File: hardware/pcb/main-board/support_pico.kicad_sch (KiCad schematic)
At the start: 7 parts, among them J702 Z88 SD Card, U701 Support Pico

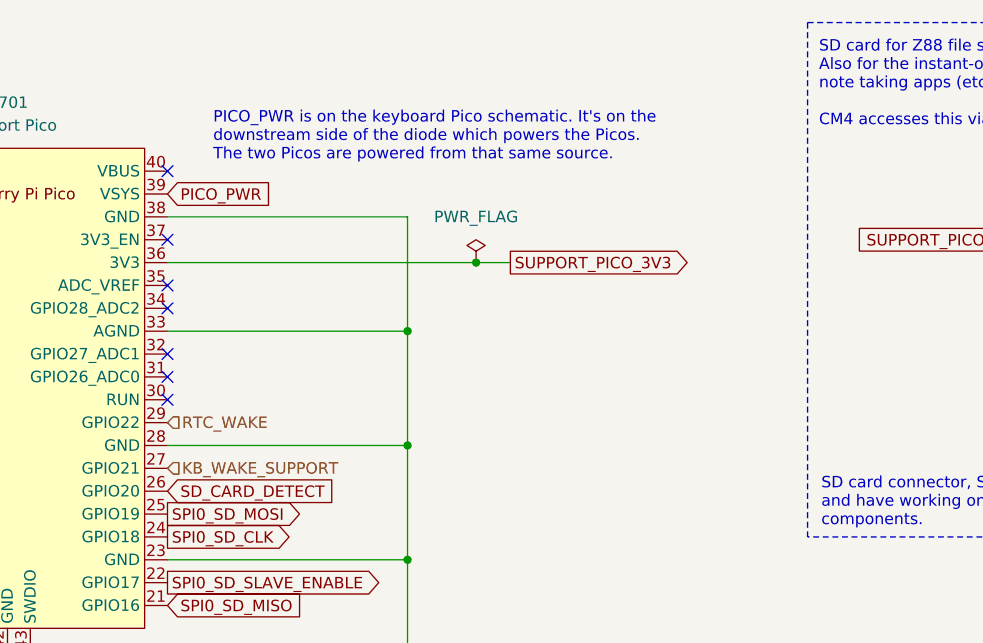
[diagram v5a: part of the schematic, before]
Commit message: more working out of the KB pico replacement
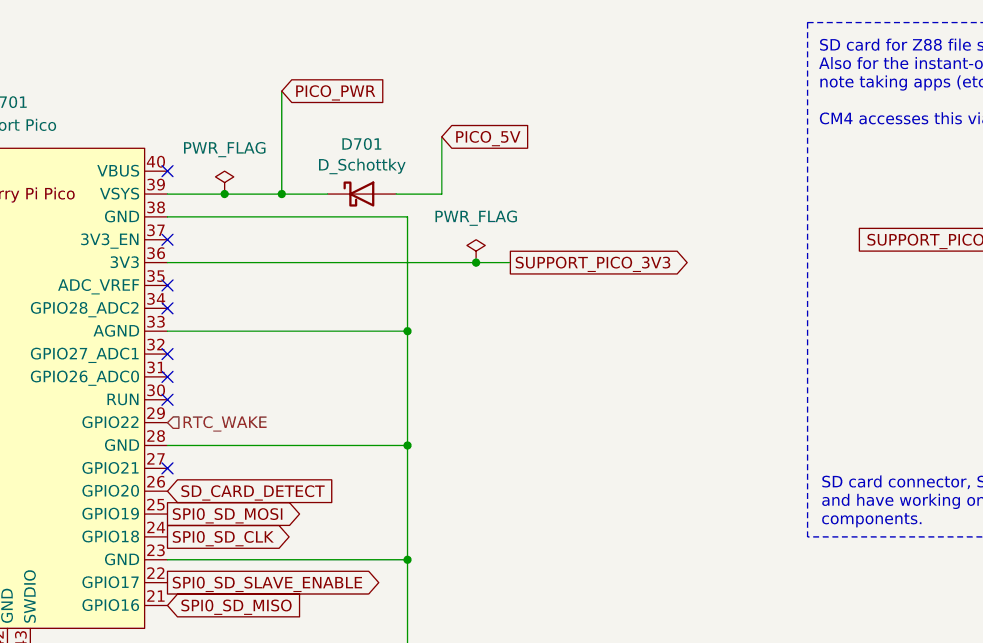
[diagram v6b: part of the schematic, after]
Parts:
- added D701: D_Schottky, Diode_SMD:D_1206_3216Metric_Pad1.42x1.75mm_HandSolder, symbol Device:D_Schottky
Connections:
- net PICO_PWR: now also D701.1 (K)
- net KB_WAKE_SUPPORT: no longer names the net of U701.27 (GPIO21)
- new net PICO_5V: D701.2 (A)
- no-connect marks 14 -> 15
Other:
- note removed: "PICO_PWR is on the keyboard Pico schematic. It's on the downstream side of the diode which powers the Picos. The two Picos are powered from that same source."
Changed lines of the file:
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@@
+	)
+	(junction
+		(at 106.68 38.1)
+		(diameter 0)
+		(color 0 0 0 0)
 	)
 	(junction
@@
 		(color 0 0 0 0)
 	)
+	(junction
+		(at 100.33 38.1)
+		(diameter 0)
+		(color 0 0 0 0)
+	)
 	(no_connect
 		(at 58.42 63.5)
@@
 	)
 	(no_connect
+		(at 93.98 68.58)
+	)
+	(no_connect
 		(at 93.98 48.26)
 	)
@@
 		)
 	)
+	(wire
+		(pts
+			(xy 93.98 38.1) (xy 100.33 38.1)
+		)
+		(stroke
+			(width 0)
+			(type default)
+		)
+	)
 	(polyline
 		(pts
@@
 	(wire
 		(pts
+			(xy 106.68 26.67) (xy 106.68 38.1)
+		)
+		(stroke
+			(width 0)
+			(type default)
+		)
+	)
+	(wire
+		(pts
+			(xy 119.38 38.1) (xy 124.46 38.1)
+		)
+		(stroke
+			(width 0)
+			(type default)
+		)
+	)
+	(wire
+		(pts
+			(xy 100.33 38.1) (xy 106.68 38.1)
+		)
+		(stroke
+			(width 0)
+			(type default)
+		)
+	)
+	(wire
+		(pts
 			(xy 132.08 45.72) (xy 128.27 45.72)
 		)
@@
 		)
 	)
+	(wire
+		(pts
+			(xy 124.46 38.1) (xy 124.46 31.75)
+		)
+		(stroke
+			(width 0)
+			(type default)
+		)
+	)
 	(polyline
 		(pts
@@
 		(pts
 			(xy 20.32 66.04) (xy 58.42 66.04)
+		)
+		(stroke
+			(width 0)
+			(type default)
+		)
+	)
+	(wire
+		(pts
+			(xy 106.68 38.1) (xy 111.76 38.1)
 		)
 		(stroke
@@
 		)
 	)
-	(text "PICO_PWR is on the keyboard Pico schematic. It's on the\ndownstream side of the diode which powers the Picos.\nThe two Picos are powered from that same source."
-		(exclude_from_sim no)
-		(at 99.06 31.75 0)
-		(effects
-			(font
-				(size 1.27 1.27)
-			)
-			(justify left)
-		)
-	)
 	(text "Card detect pin on our components"
 		(exclude_from_sim no)
@@
 		)
 	)
+	(global_label "PICO_5V"
+		(shape input)
+		(at 124.46 31.75 0)
+		(fields_autoplaced yes)
+		(effects
+			(font
+				(size 1.27 1.27)
+			)
+			(justify left)
+		)
+		(property "Intersheetrefs" "${INTERSHEET_REFS}"
+			(at 134.532 31.75 0)
+			(effects
+				(font
+					(size 1.27 1.27)
+				)
+				(justify left)
+				(hide yes)
+			)
+		)
+	)
 	(global_label "SUPPORT_PICO_3V3"
 		(shape output)
@@
 		)
 	)
-	(global_label "PICO_PWR"
-		(shape input)
-		(at 93.98 38.1 0)
-		(fields_autoplaced yes)
-		(effects
-			(font
-				(size 1.27 1.27)
-			)
-			(justify left)
-		)
-		(property "Intersheetrefs" "${INTERSHEET_REFS}"
-			(at 105.7453 38.1 0)
-			(effects
-				(font
-					(size 1.27 1.27)
-				)
-				(justify left)
-				(hide yes)
-			)
-		)
-	)
 	(global_label "MAIN_I2C_CLK"
 		(shape output)
@@
 		)
 	)
+	(global_label "PICO_PWR"
+		(shape input)
+		(at 106.68 26.67 0)
+		(fields_autoplaced yes)
+		(effects
+			(font
+				(size 1.27 1.27)
+			)
+			(justify left)
+		)
+		(property "Intersheetrefs" "${INTERSHEET_REFS}"
+			(at 118.5274 26.5906 0)
+			(effects
+				(font
+					(size 1.27 1.27)
+				)
+				(justify left)
+				(hide yes)
+			)
+		)
+	)
 	(global_label "SPI0_SD_SLAVE_ENABLE"
 		(shape output)
@@
 		(shape input)
 		(at 93.98 63.5 0)
-		(effects
-			(font
-				(size 1.27 1.27)
-			)
-			(justify left)
-		)
-	)
-	(hierarchical_label "KB_WAKE_SUPPORT"
-		(shape input)
-		(at 93.98 68.58 0)
 		(effects
 			(font
@@
 					(unit 1)
 				)
+			)
+		)
+	)
+	(symbol
+		(lib_id "Device:D_Schottky")
+		(at 115.57 38.1 0)
+		(unit 1)
+		(exclude_from_sim no)
+		(in_bom yes)
+		(on_board yes)
+		(dnp no)
+		(property "Reference" "D701"
+			(at 115.57 32.5882 0)
+			(effects
+				(font
+					(size 1.27 1.27)
+				)
+			)
+		)
+		(property "Value" "D_Schottky"
+			(at 115.57 34.8996 0)
+			(effects
+				(font
+					(size 1.27 1.27)
+				)
+			)
+		)
+		(property "Footprint" "Diode_SMD:D_1206_3216Metric_Pad1.42x1.75mm_HandSolder"
+			(at 115.57 38.1 0)
+			(effects
+				(font
+					(size 1.27 1.27)
+				)
+				(hide yes)
+			)
+		)
+		(property "Datasheet" "~"
+			(at 115.57 38.1 0)
+			(effects
+				(font
+					(size 1.27 1.27)
+				)
+				(hide yes)
+			)
+		)
+		(property "Description" ""
+			(at 115.57 38.1 0)
+			(effects
+				(font
+					(size 1.27 1.27)
+				)
+				(hide yes)
+			)
+		)
+		(pin "1"
+		)
+		(pin "2"
+		)
+		(instances
+			(project "z88_new"
+				(path "/fdce8012-5f35-4f58-8abb-80214b4af8fe/473923ee-4723-4e62-9c3b-b8c36a40674a"
+					(reference "D701")
+					(unit 1)
+				)
+			)
+		)
+	)
+	(symbol
+		(lib_id "power:PWR_FLAG")
+		(at 100.33 38.1 0)
+		(unit 1)
+		(exclude_from_sim no)
+		(in_bom yes)
+		(on_board yes)
+		(dnp no)
+		(fields_autoplaced yes)
+		(property "Reference" "#FLG702"
+			(at 100.33 36.195 0)
+			(effects
+				(font
+					(size 1.27 1.27)
+				)
+				(hide yes)
+			)
+		)
+		(property "Value" "PWR_FLAG"
+			(at 100.33 33.02 0)
+			(effects
+				(font
+					(size 1.27 1.27)
+				)
+			)
+		)
+		(property "Footprint" ""
+			(at 100.33 38.1 0)
+			(effects
+				(font
+					(size 1.27 1.27)
+				)
+				(hide yes)
+			)
+		)
+		(property "Datasheet" "~"
+			(at 100.33 38.1 0)
+			(effects
+				(font
+					(size 1.27 1.27)
+				)
+				(hide yes)
+			)
+		)
+		(property "Description" "Special symbol for telling ERC where power comes from"
+			(at 100.33 38.1 0)
+			(effects
+				(font
+					(size 1.27 1.27)
+				)
+				(hide yes)
+			)
+		)
+		(pin "1"
+		)
+		(instances
+			(project "z88_new"
+				(path "/fdce8012-5f35-4f58-8abb-80214b4af8fe/473923ee-4723-4e62-9c3b-b8c36a40674a"
+					(reference "#FLG702")
+					(unit 1)
+				)

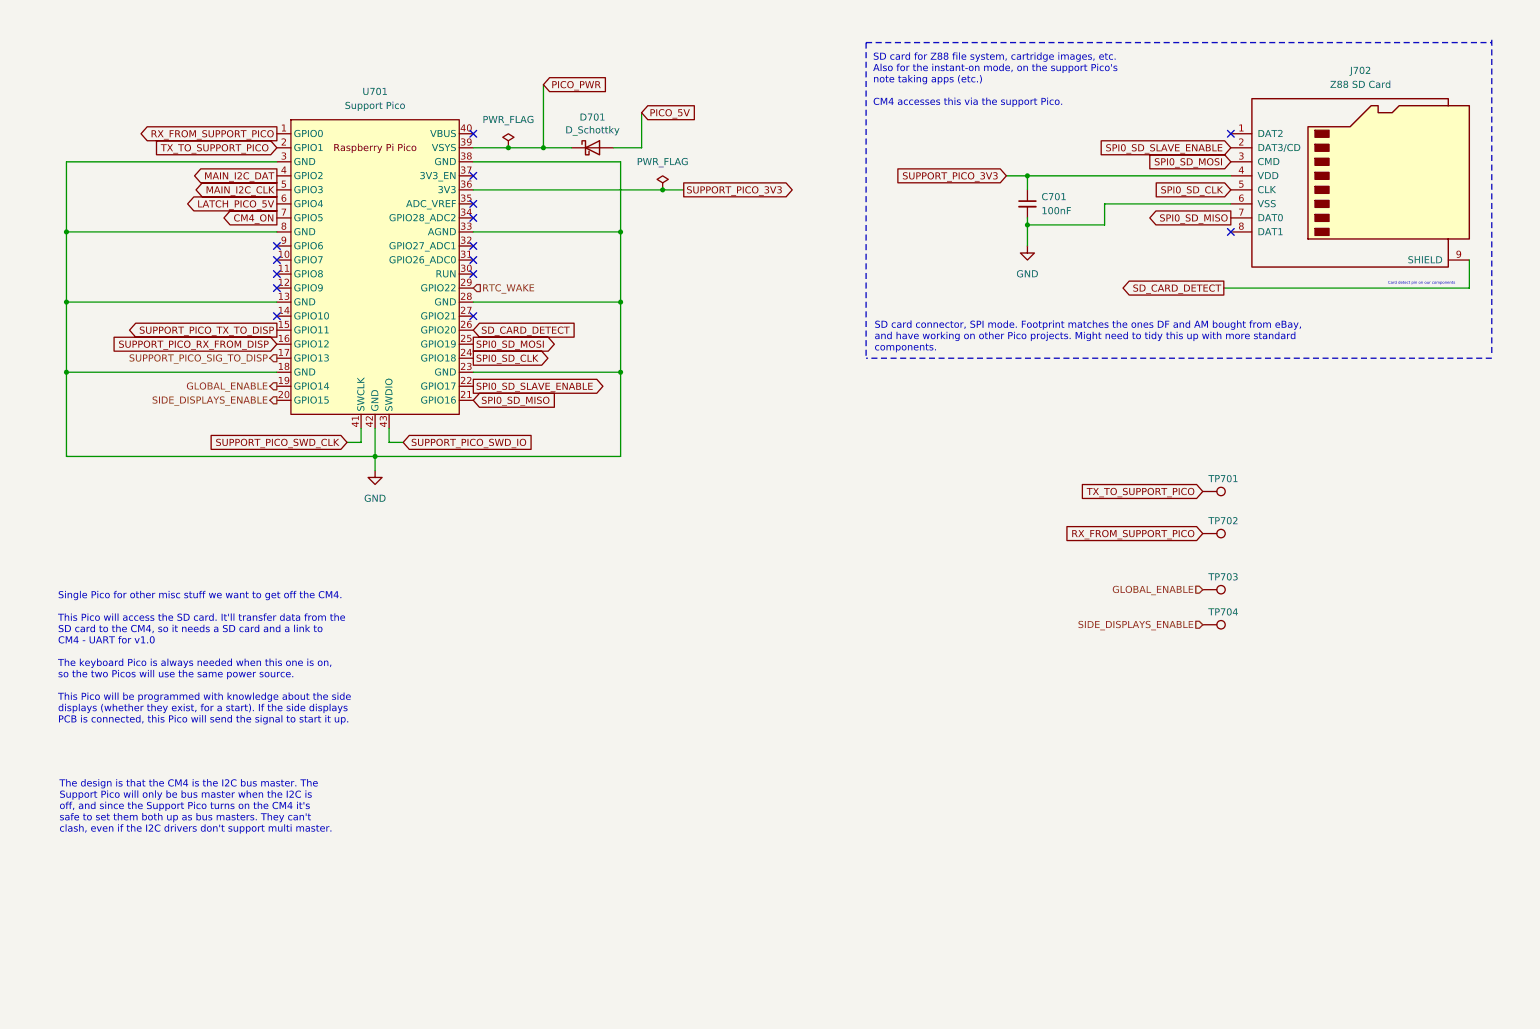
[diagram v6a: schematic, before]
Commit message: start the support pico rp2040 replacement
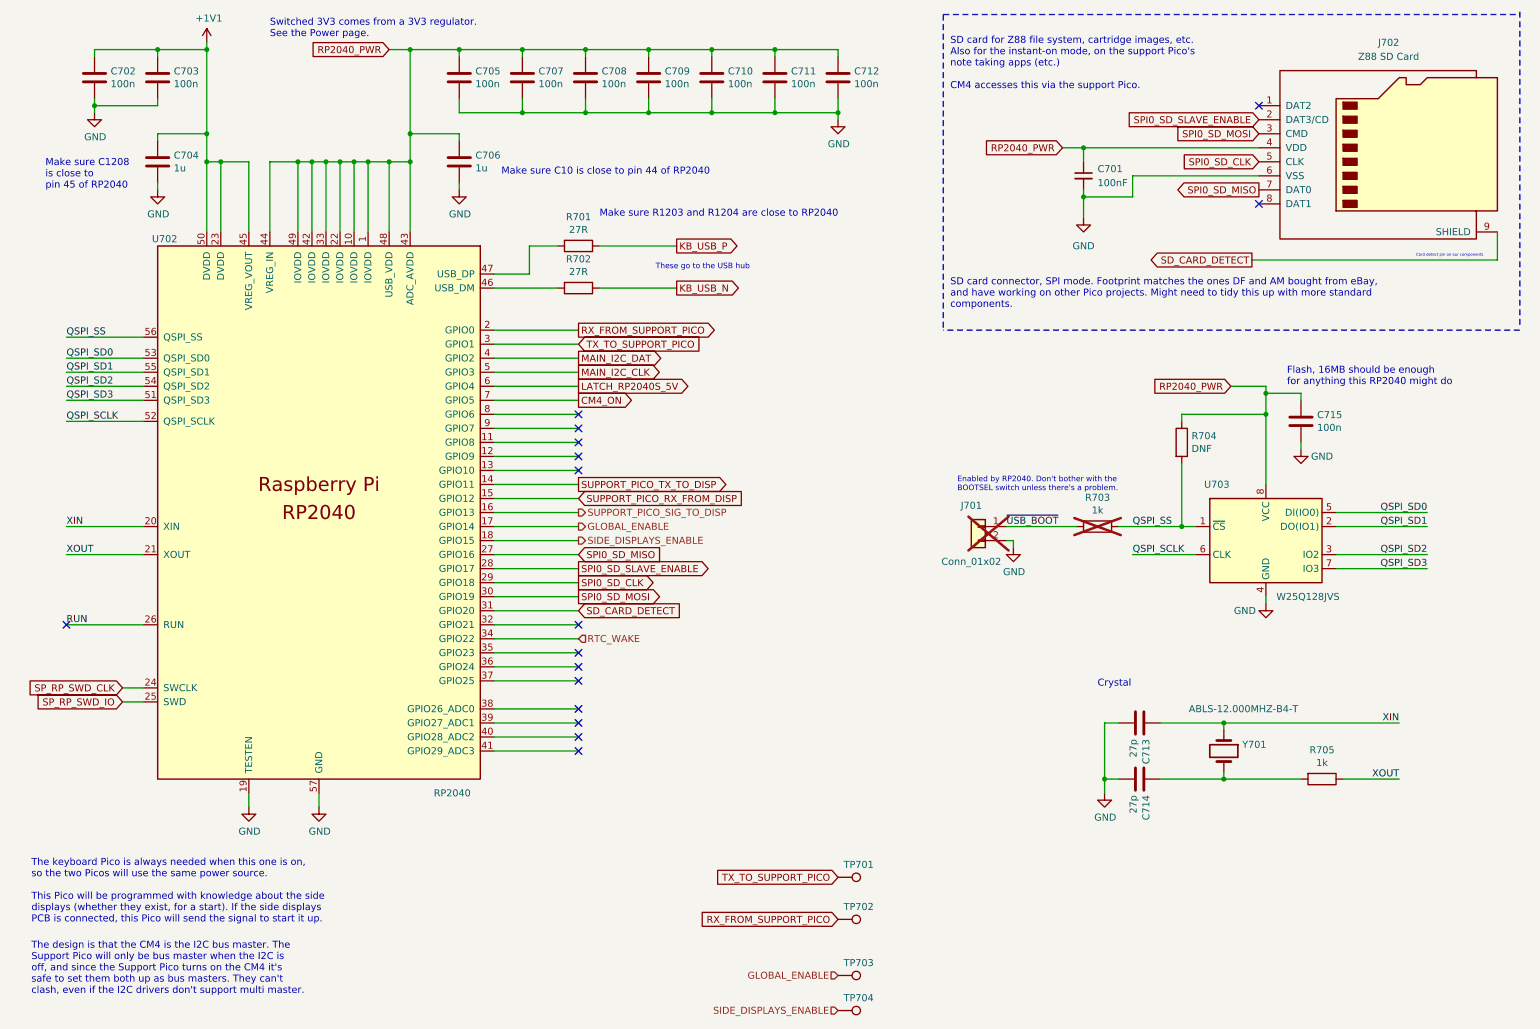
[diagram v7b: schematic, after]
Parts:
- removed D701: D_Schottky, Diode_SMD:D_1206_3216Metric_Pad1.42x1.75mm_HandSolder, symbol Device:D_Schottky
- removed U701: Support Pico, Pico:RPi_Pico_SMD_TH, symbol RP Pico:Pico
- added C702, C703, C705, C707, C708, C709, C710, C711, C712, C715: 100n, Capacitor_SMD:C_0402_1005Metric, symbol Device:C
- added C704, C706: 1u, Capacitor_SMD:C_0402_1005Metric, symbol Device:C
- added C713, C714: 27p, Capacitor_SMD:C_0402_1005Metric, symbol Device:C
- added J701: Conn_01x02, Connector_PinHeader_2.54mm:PinHeader_1x02_P2.54mm_Vertical, symbol Connector_Generic:Conn_01x02
- added R701, R702: 27R, Capacitor_SMD:C_0402_1005Metric, symbol Device:R
- added R703, R705: 1k, Capacitor_SMD:C_0402_1005Metric, symbol Device:R
- added R704: DNF, Capacitor_SMD:C_0402_1005Metric, symbol Device:R
- added U702: RP2040, RP2040_minimal:RP2040-QFN-56, symbol MCU_RaspberryPi_RP2040:RP2040
- added U703: W25Q128JVS, Package_SO:SOIC-8_5.23x5.23mm_P1.27mm, symbol Memory_Flash:W25Q128JVS
- added Y701: ABLS-12.000MHZ-B4-T, RP2040_minimal:Crystal_SMD_HC49-US, symbol Device:Crystal
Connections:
- net CM4_ON: now also U702.7 (GPIO5)
- net GLOBAL_ENABLE: now also U702.17 (GPIO14)
- net GND: now also C702.2, C703.2, C704.2, C705.2, C706.2, C707.2, C708.2, C709.2, C710.2, C711.2, C712.2, C713.2, C714.2, C715.2, J701.2 (Pin_2), U702.19 (TESTEN), U702.57 (GND), U703.4 (GND)
- net MAIN_I2C_CLK: now also U702.5 (GPIO3)
- net MAIN_I2C_DAT: now also U702.4 (GPIO2)
- net RTC_WAKE: now also U702.34 (GPIO22)
- net RX_FROM_SUPPORT_PICO: now also U702.2 (GPIO0)
- net SD_CARD_DETECT: now also U702.31 (GPIO20)
- net SIDE_DISPLAYS_ENABLE: now also U702.18 (GPIO15)
- net SPI0_SD_CLK: now also U702.29 (GPIO18)
- net SPI0_SD_MISO: now also U702.27 (GPIO16)
- net SPI0_SD_MOSI: now also U702.30 (GPIO19)
- net SPI0_SD_SLAVE_ENABLE: now also U702.28 (GPIO17)
- net SUPPORT_PICO_RX_FROM_DISP: now also U702.15 (GPIO12)
- net SUPPORT_PICO_SIG_TO_DISP: now also U702.16 (GPIO13)
- net SUPPORT_PICO_TX_TO_DISP: now also U702.14 (GPIO11)
- net TX_TO_SUPPORT_PICO: now also U702.3 (GPIO1)
- net SUPPORT_PICO_3V3 renamed RP2040_PWR
- net RP2040_PWR: now also C705.1, C706.1, C707.1, C708.1, C709.1, C710.1, C711.1, C712.1, C715.1, R704.1, U702.1 (IOVDD), U702.10 (IOVDD), U702.22 (IOVDD), U702.33 (IOVDD), U702.42 (IOVDD), U702.43 (ADC_AVDD), U702.44 (VREG_IN), U702.48 (USB_VDD), U702.49 (IOVDD), U703.8 (VCC)
- new net: C714.1, R705.2, Y701.2
- new net: R702.2, U702.46 (USB_DM)
- new net: R701.2, U702.47 (USB_DP)
- new net +1V1: C702.1, C703.1, C704.1, U702.23 (DVDD), U702.45 (VREG_VOUT), U702.50 (DVDD)
- new net KB_USB_N: R702.1
- new net KB_USB_P: R701.1
- new net LATCH_RP2040S_5V: U702.6 (GPIO4)
- new net QSPI_SCLK: U702.52 (QSPI_SCLK), U703.6 (CLK)
- new net QSPI_SD0: U702.53 (QSPI_SD0), U703.5 (DI(IO0))
- new net QSPI_SD1: U702.55 (QSPI_SD1), U703.2 (DO(IO1))
- new net QSPI_SD2: U702.54 (QSPI_SD2), U703.3 (IO2)
- new net QSPI_SD3: U702.51 (QSPI_SD3), U703.7 (IO3)
- new net QSPI_SS: R703.1, R704.2, U702.56 (QSPI_SS), U703.1 (~{CS})
- new net RUN: U702.26 (RUN)
- new net SP_RP_SWD_CLK: U702.24 (SWCLK)
- new net SP_RP_SWD_IO: U702.25 (SWD)
- new net XIN: C713.1, U702.20 (XIN), Y701.1
- new net XOUT: R705.1, U702.21 (XOUT)
- new net ~{USB_BOOT}: J701.1 (Pin_1), R703.2
- no-connect marks 15 -> 16
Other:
- note added: "Crystal"
- note added: "Enabled by RP2040. Don't bother with the BOOTSEL switch unless there's a problem."
- note added: "Flash, 16MB should be enough for anything this RP2040 might do"
- note added: "Make sure C10 is close to pin 44 of RP2040"
- note added: "Make sure C1208 is close to pin 45 of RP2040"
- note added: "Make sure R1203 and R1204 are close to RP2040"
- note added: "Switched 3V3 comes from a 3V3 regulator. See the Power page."
- note added: "The keyboard Pico is always needed when this one is on, so the two Picos will use the same power source. This Pico will be programmed with knowledge about the side displays (whether they exist, for a start). If the side displays PCB is connected, this Pico will send the signal to start it up."
- note added: "These go to the USB hub"
- note removed: "Single Pico for other misc stuff we want to get off the CM4. This Pico will access the SD card. It'll transfer data from the SD card to the CM4, so it needs a SD card and a link to CM4 - UART for v1.0 The keyboard Pico is always needed when this one is on, so the two Picos will use the same power source. This Pico will be programmed with knowledge about the side displays (whether they exist, for 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"
- moved on the sheet: C701, J702, TP701, TP702, TP703, TP704

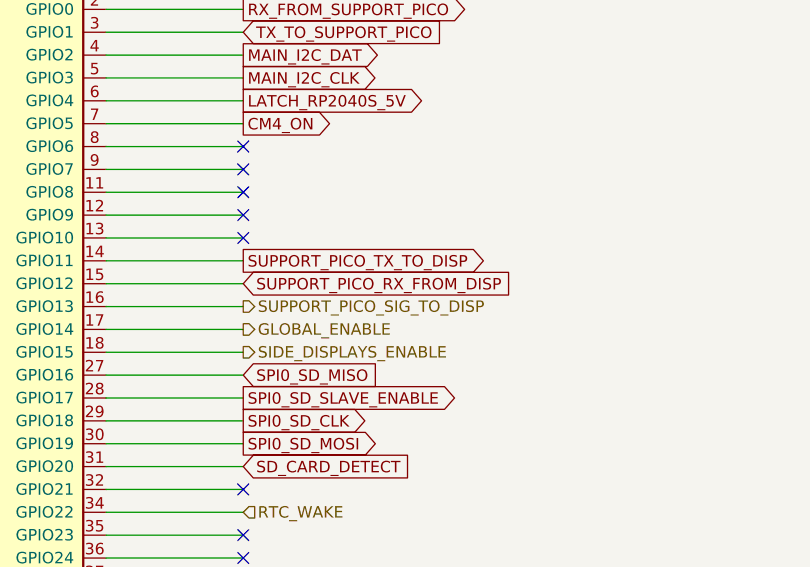
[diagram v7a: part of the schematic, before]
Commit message: rename the pico bits to RP2040, still a few things to check
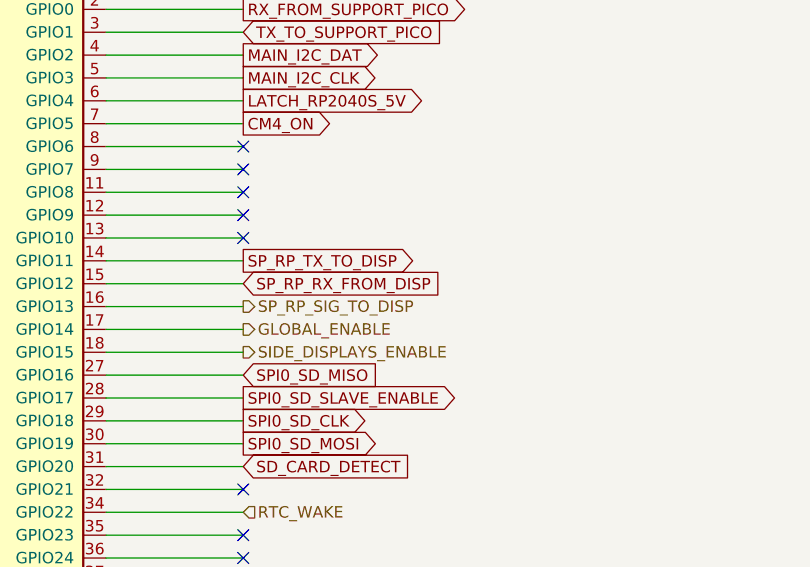
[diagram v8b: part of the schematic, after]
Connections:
- net SUPPORT_PICO_RX_FROM_DISP renamed SP_RP_RX_FROM_DISP
- net SUPPORT_PICO_SIG_TO_DISP renamed SP_RP_SIG_TO_DISP
- net SUPPORT_PICO_TX_TO_DISP renamed SP_RP_TX_TO_DISP
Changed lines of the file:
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@@
 		)
 	)
-	(global_label "SUPPORT_PICO_TX_TO_DISP"
+	(global_label "SP_RP_TX_TO_DISP"
 		(shape output)
 		(at 113.03 99.06 0)
@@
 		)
 		(property "Intersheetrefs" "${INTERSHEET_REFS}"
-			(at 141.1843 99.06 0)
+			(at 133.0804 99.06 0)
 			(effects
 				(font
@@
 		)
 	)
-	(global_label "SUPPORT_PICO_RX_FROM_DISP"
+	(global_label "SP_RP_RX_FROM_DISP"
 		(shape input)
 		(at 113.03 101.6 0)
@@
 		)
 		(property "Intersheetrefs" "${INTERSHEET_REFS}"
-			(at 144.3291 101.6 0)
+			(at 136.2252 101.6 0)
 			(effects
 				(font
@@
 		)
 	)
-	(hierarchical_label "SUPPORT_PICO_SIG_TO_DISP"
+	(hierarchical_label "SP_RP_SIG_TO_DISP"
 		(shape output)
 		(at 113.03 104.14 0)
